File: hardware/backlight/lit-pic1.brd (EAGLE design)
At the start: 58.4 x 68.2 mm, 39 parts, among them J1 1x8 header, U1 ATTINY45-20SU

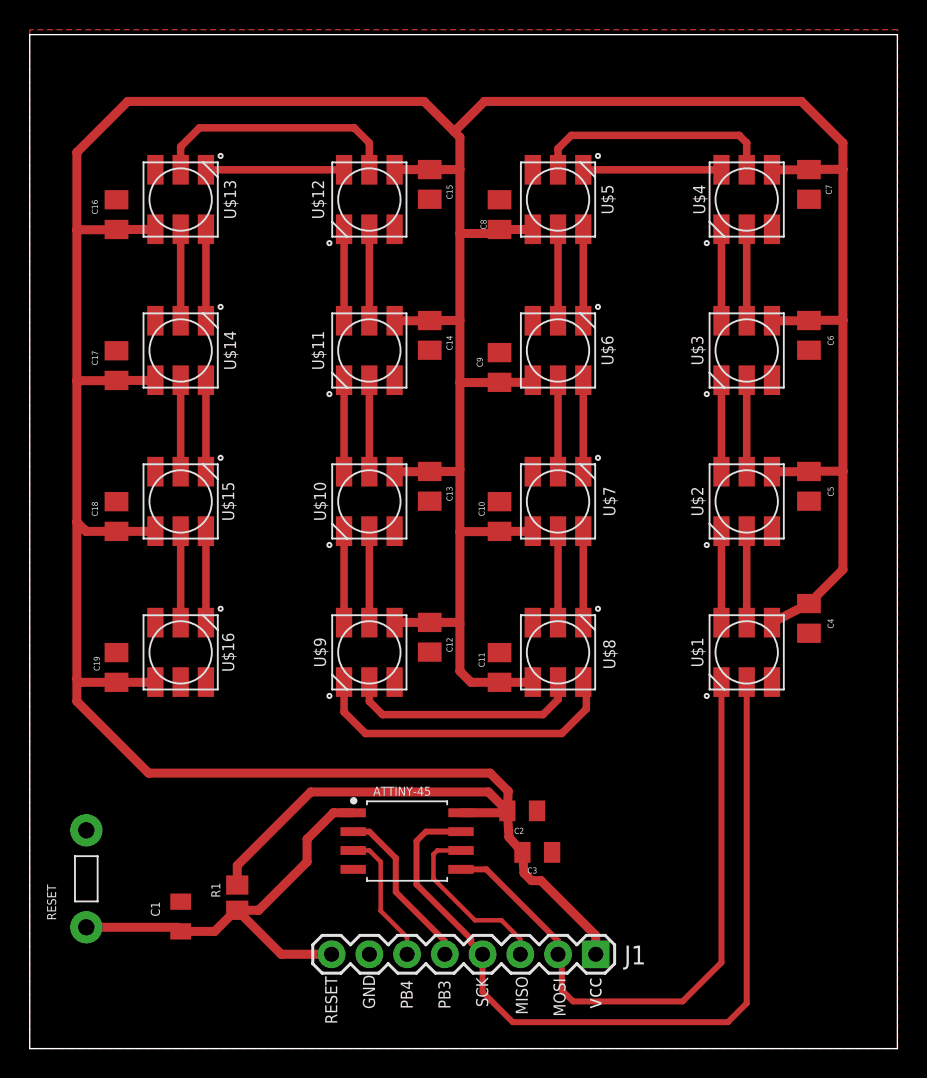
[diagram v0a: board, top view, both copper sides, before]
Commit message: thicked traces and started real board
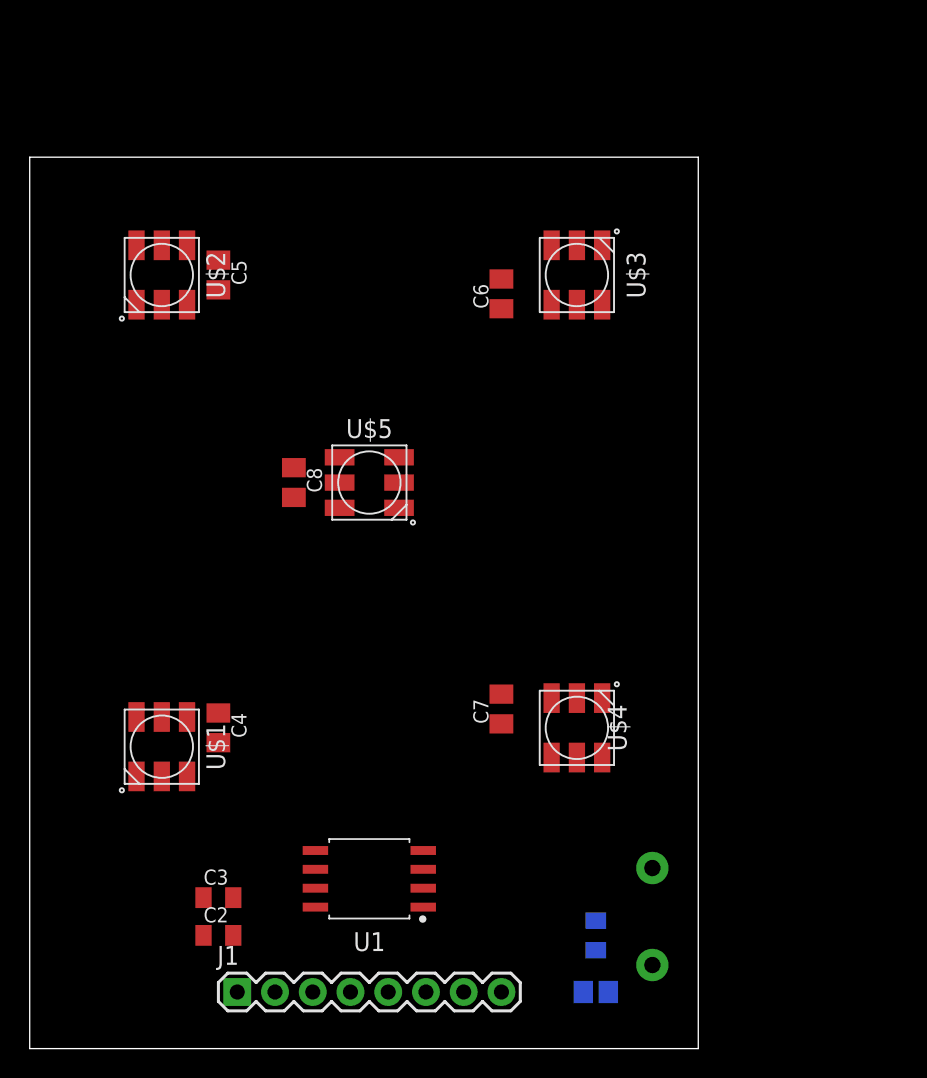
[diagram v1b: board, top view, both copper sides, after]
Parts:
- removed C10, C11, C12, C13, C14, C15, C16, C17, C18, C19, C9: 15pF, passives:C0805K
- removed U$10, U$11, U$12, U$13, U$14, U$15, U$16, U$6, U$7, U$8, U$9: APA1025050, leds:APA102_5050
- moved C5 42.2 mm to (12.7, 52.1)
- moved U$2 42.2 mm to (8.89, 52.1)
- moved C7 40.9 mm to (31.8, 22.9), turned to 90 degrees
- moved C4 40.4 mm to (12.7, 21.6)
- moved U$1 39.9 mm to (8.89, 20.3)
- moved RESET 38.2 mm to (41.9, 8.89), flipped to the bottom
- moved U$4 37.4 mm to (36.8, 21.6), turned to 270 degrees
- moved C1 28.0 mm to (38.1, 7.62), flipped to the bottom
- moved R1 25.0 mm to (38.1, 3.81), flipped to the bottom, turned to 0 degrees
- moved J1 24.3 mm to (14.0, 3.81), turned to 0 degrees
- moved U$5 22.9 mm to (22.9, 38.1), turned to 180 degrees
- moved C8 22.7 mm to (17.8, 38.1), turned to 270 degrees
- moved C2 22.1 mm to (12.7, 7.62), turned to 0 degrees
- moved C3 21.7 mm to (12.7, 10.2), turned to 0 degrees
- moved C6 20.9 mm to (31.8, 50.8), turned to 90 degrees
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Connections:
- removed net N$1: U$8.2, U$9.5
- removed net N$13: U$5.2, U$6.5
- removed net N$14: U$5.3, U$6.4
- removed net N$17: U$7.2, U$8.5
- removed net N$18: U$7.3, U$8.4
- removed net N$19: U$6.2, U$7.5
- removed net N$2: U$8.3, U$9.4
- removed net N$20: U$6.3, U$7.4
- removed net N$22: U$12.3, U$13.4
- removed net N$23: U$10.5, U$9.2
- removed net N$24: U$10.4, U$9.3
- removed net N$25: U$12.2, U$13.5
- removed net N$27: U$11.2, U$12.5
- removed net N$28: U$11.3, U$12.4
- removed net N$29: U$10.2, U$11.5
- removed net N$30: U$10.3, U$11.4
- removed net N$33: U$13.2, U$14.5
- removed net N$34: U$13.3, U$14.4
- removed net N$37: U$15.2, U$16.5
- removed net N$38: U$15.3, U$16.4
- removed net N$39: U$14.2, U$15.5
- removed net N$40: U$14.3, U$15.4
- net GND: no longer C10.2, C11.2, C12.2, C13.2, C14.2, C15.2, C16.2, C17.2, C18.2, C19.2, C9.2, U$10.6, U$11.6, U$12.6, U$13.6, U$14.6, U$15.6, U$16.6, U$6.6, U$7.6, U$8.6, U$9.6
- net VCC: no longer C10.1, C11.1, C12.1, C13.1, C14.1, C15.1, C16.1, C17.1, C18.1, C19.1, C9.1, U$10.1, U$11.1, U$12.1, U$13.1, U$14.1, U$15.1, U$16.1, U$6.1, U$7.1, U$8.1, U$9.1
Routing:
- net VCC: track 308.3 -> 0.00 mm
- net PB2-SCK: track 56.0 -> 0.00 mm
- net PB0-MOSI: track 43.0 -> 0.00 mm
- net RESET: track 30.2 -> 0.00 mm
- net N$2: track 21.5 -> 0.00 mm
- net N$25: track 17.0 -> 0.00 mm
- net N$42: track 16.5 -> 0.00 mm
- net N$1: track 16.0 -> 0.00 mm
- net PB1-MISO: track 12.1 -> 0.00 mm
- net PB3: track 11.4 -> 0.00 mm
- net N$41: track 9.30 -> 0.00 mm
- net N$22: track 9.30 -> 0.00 mm
- net PB4: track 9.13 -> 0.00 mm
- net N$9: track 6.16 -> 0.00 mm
- net N$40: track 6.16 -> 0.00 mm
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- removed copper zone on layer 1, net GND
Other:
- board size 58.4 x 68.2 mm -> 45 x 60 mm
- board text removed: "ATTINY-45"
- board text removed: "GND"
- board text removed: "MISO"
- board text removed: "MOSI"
- board text removed: "PB3"
- board text removed: "PB4"
- board text removed: "RESET"
- board text removed: "SCK"
- board text removed: "vcc"
